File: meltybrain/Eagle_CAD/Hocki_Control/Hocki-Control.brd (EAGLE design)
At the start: 87 x 44 mm, 103 parts, among them J1 SM05B-SRSS-TB(LF)(SN), J2 SM05B-SRSS-TB(LF)(SN), U1 TEENSY_4.1, U10 TLV3502AIDCNR, U11 NL27WZ32USG, U12 NL27WZ32USG, U13 HMC1052L-TR, U14 LMV358, U15 IRF7509, U16 TMUX1219DCKR, U17 LMV358, U18 LMV358, U19 AP2210K-3.3TRG1, U2 ADXL375, U20 AP2210K-5.0TRG1, U3 ADXL375, U4 ADXL375, U5 ADXL375, U6 LMH6612MAX/NOPB, U7 LMH6612MAX/NOPB, U8 LMH6612MAX/NOPB, U9 LMH6612MAX/NOPB

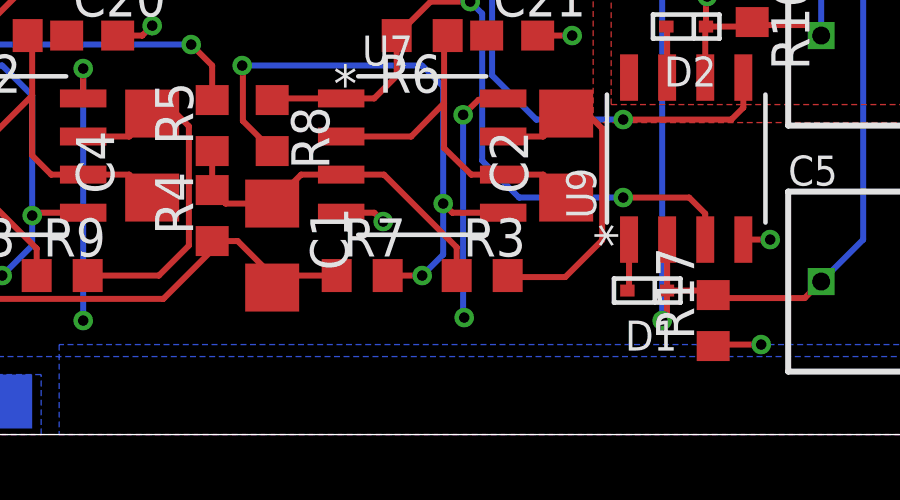
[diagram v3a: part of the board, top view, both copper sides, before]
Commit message: fixed 10k bandpass
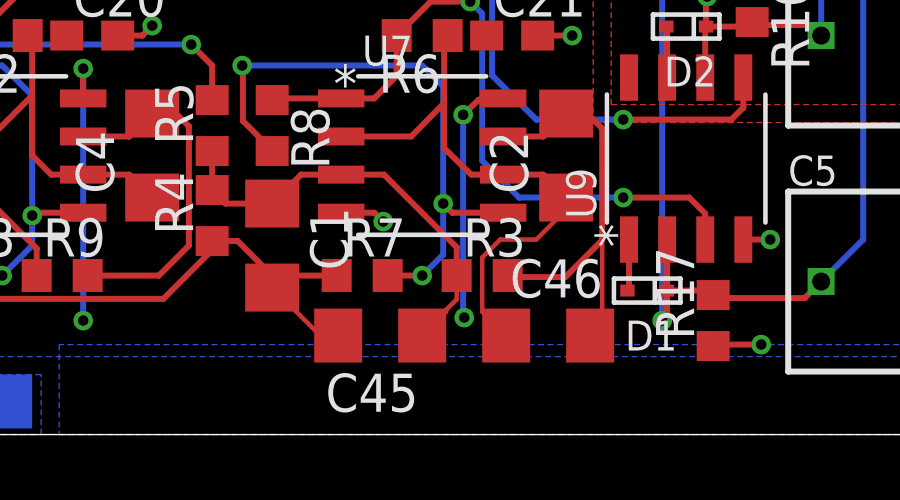
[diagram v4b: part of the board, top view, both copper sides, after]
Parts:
- added C45, C46: 47n, rcl:C1206
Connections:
- net 1.66V_REF_BUF: now also C45.2
- net 10K_FB: now also C46.2
- net 10K_IN: now also C45.1
- net N$4: now also C46.1
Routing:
- net N$4: track 12.5 -> 19.2 mm
- net 10K_FB: track 11.2 -> 14.6 mm
- net 1.66V_REF_BUF: track 29.0 -> 31.9 mm
- net 10K_IN: track 12.0 -> 14.5 mm
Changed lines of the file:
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@@
 <drawing>
 <settings>
-<setting alwaysvectorfont="yes"/>
+<setting alwaysvectorfont="no"/>
 <setting verticaltext="up"/>
 </settings>
@@
 <attribute name="VALUE" x="-26.205" y="-19.065" size="1.27" layer="27" rot="R270"/>
 </element>
+<element name="C45" library="rcl" library_urn="urn:adsk.eagle:library:334" package="C1206" package3d_urn="urn:adsk.eagle:package:23618/2" value="47n" x="6.3" y="-21.7" smashed="yes" rot="R180">
+<attribute name="NAME" x="7.57" y="-22.97" size="1.27" layer="25" rot="R180"/>
+<attribute name="POPULARITY" value="24" x="6.3" y="-21.7" size="1.778" layer="27" rot="R180" display="off"/>
+<attribute name="SPICEPREFIX" value="C" x="6.3" y="-21.7" size="1.778" layer="27" rot="R180" display="off"/>
+<attribute name="VALUE" x="7.57" y="-19.16" size="1.27" layer="27" rot="R180"/>
+</element>
+<element name="C46" library="rcl" library_urn="urn:adsk.eagle:library:334" package="C1206" package3d_urn="urn:adsk.eagle:package:23618/2" value="47n" x="11.9" y="-21.7" smashed="yes">
+<attribute name="NAME" x="10.63" y="-20.43" size="1.27" layer="25"/>
+<attribute name="POPULARITY" value="24" x="11.9" y="-21.7" size="1.778" layer="27" display="off"/>
+<attribute name="SPICEPREFIX" value="C" x="11.9" y="-21.7" size="1.778" layer="27" display="off"/>
+<attribute name="VALUE" x="10.63" y="-24.24" size="1.27" layer="27"/>
+</element>
 </elements>
 <signals>
@@
 <wire x1="12.471025" y1="-19.75" x2="13.7" y2="-18.521025" width="0.2" layer="1"/>
 <wire x1="13.7" y1="-18.521025" x2="13.7" y2="-14.8" width="0.2" layer="1"/>
+<contactref element="C46" pad="2"/>
+<wire x1="13.3" y1="-21.7" x2="13.7" y2="-21.3" width="0.1524" layer="1"/>
+<wire x1="13.7" y1="-21.3" x2="13.7" y2="-18.521025" width="0.1524" layer="1"/>
 </signal>
 <signal name="N$4">
@@
 <wire x1="10.4" y1="-16.335" x2="11.735" y2="-16.335" width="0.2" layer="1"/>
 <wire x1="11.735" y1="-16.335" x2="12.5" y2="-17.1" width="0.2" layer="1"/>
+<contactref element="C46" pad="1"/>
+<wire x1="10.5" y1="-21.7" x2="9.7068" y2="-20.9068" width="0.1524" layer="1"/>
+<wire x1="9.7068" y1="-20.9068" x2="9.7068" y2="-20.84865" width="0.1524" layer="1"/>
+<wire x1="9.7068" y1="-20.84865" x2="9.7" y2="-20.84185" width="0.1524" layer="1"/>
+<wire x1="9.7" y1="-19.1" x2="10.3" y2="-18.5" width="0.1524" layer="1"/>
+<wire x1="10.3" y1="-18.5" x2="11.5" y2="-18.5" width="0.1524" layer="1"/>
+<wire x1="11.5" y1="-18.5" x2="12.5" y2="-17.5" width="0.1524" layer="1"/>
+<wire x1="12.5" y1="-17.5" x2="12.5" y2="-17.1" width="0.1524" layer="1"/>
+<wire x1="9.7" y1="-20.84185" x2="9.7" y2="-19.1" width="0.1524" layer="1"/>
 </signal>
 <signal name="10K_IN">
@@
 <wire x1="1.15" y1="-17.3" x2="0.7" y2="-16.85" width="0.2" layer="1"/>
 <wire x1="0.7" y1="-16.85" x2="0.7" y2="-15.55" width="0.2" layer="1"/>
+<contactref element="C45" pad="1"/>
+<wire x1="7.7" y1="-21.7" x2="8.4932" y2="-20.9068" width="0.1524" layer="1"/>
+<wire x1="8.4932" y1="-20.9068" x2="8.4932" y2="-20.84865" width="0.1524" layer="1"/>
+<wire x1="8.85" y1="-20.49185" x2="8.85" y2="-19.7" width="0.1524" layer="1"/>
+<wire x1="8.4932" y1="-20.84865" x2="8.85" y2="-20.49185" width="0.1524" layer="1"/>
 </signal>
 <signal name="10K_OUT">
@@
 <wire x1="-10.523" y1="-20.477" x2="-11.1" y2="-19.9" width="0.2" layer="1"/>
 <wire x1="-0.927" y1="-20.477" x2="-10.523" y2="-20.477" width="0.2" layer="1"/>
+<contactref element="C45" pad="2"/>
+<wire x1="4.9" y1="-21.7" x2="4.3" y2="-21.7" width="0.1524" layer="1"/>
+<wire x1="4.3" y1="-21.7" x2="2.7" y2="-20.1" width="0.1524" layer="1"/>
 </signal>
 <signal name="N$2">

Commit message: forgot to save before pushing...
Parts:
- J1, J2: value SM05B-SRSS-TB(LF)(SN) -> SM03B-SRSS-TB(LF)(SN); device Hocki_Library:SM05B-SRSS-TB(LF)(SN) -> Hocki_Library:SM03B-SRSS-TB(LF)(SN)
- moved J1 9.45 mm to (-18.5, -22.2), flipped to the top
- moved J2 7.50 mm to (-24.5, -22.2), flipped to the top
- moved C42 6.04 mm to (-21.8, -19.8), turned to 0 degrees
- moved C44 5.10 mm to (-26.5, -15.1), turned to 180 degrees
- moved C18 3.58 mm to (-13.2, -23.4), turned to 0 degrees
- moved C41 2.21 mm to (-29.4, -17.6)
- moved U20 2.21 mm to (-26.5, -17.6)
- moved U16 1.41 mm to (-14.4, -20.8)
- moved R2 1.00 mm to (-17.4, -19.8)
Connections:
- removed net IR_BOTTOM_A0: J2.3, U1.35
- removed net IR_BOTTOM_A1: J2.4, U1.34
- removed net IR_TOP_A0: J1.3, U1.37
- removed net IR_TOP_A1: J1.4, U1.36
- net 5V: now also J1.S1, J1.S2, J2.S1, J2.S2
- net 9V: no longer J1.S1, J1.S2, J2.S1, J2.S2
- net GND: now also J1.3, J2.3; no longer J1.5, J2.5
- net IR_SEL: now also U1.37; no longer U1.33
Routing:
- net IR_TOP_A1: track 24.2 -> 0.00 mm
- net IR_BOTTOM_A0: track 24.1 -> 0.00 mm
- net IR_TOP_A0: track 23.6 -> 0.00 mm
- net IR_BOTTOM_A1: track 23.0 -> 0.00 mm
- net IR_BOTTOM: track 5.14 -> 10.8 mm, vias 1 -> 0
- net IR_SEL: track 31.0 -> 26.2 mm
- net 9V: track 8.87 -> 11.8 mm, vias 0 -> 2
- net GND: track 105.4 -> 103.1 mm, vias 70 -> 72
- net N$8: track 2.04 -> 3.07 mm
- net IR_TOP: track 7.36 -> 6.50 mm, vias 1 -> 0
- net VG_SIGNAL: track 12.1 -> 11.5 mm
- removed copper zone on layer 16, net 9V
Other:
- board size 87 x 44 mm -> 90 x 46 mm

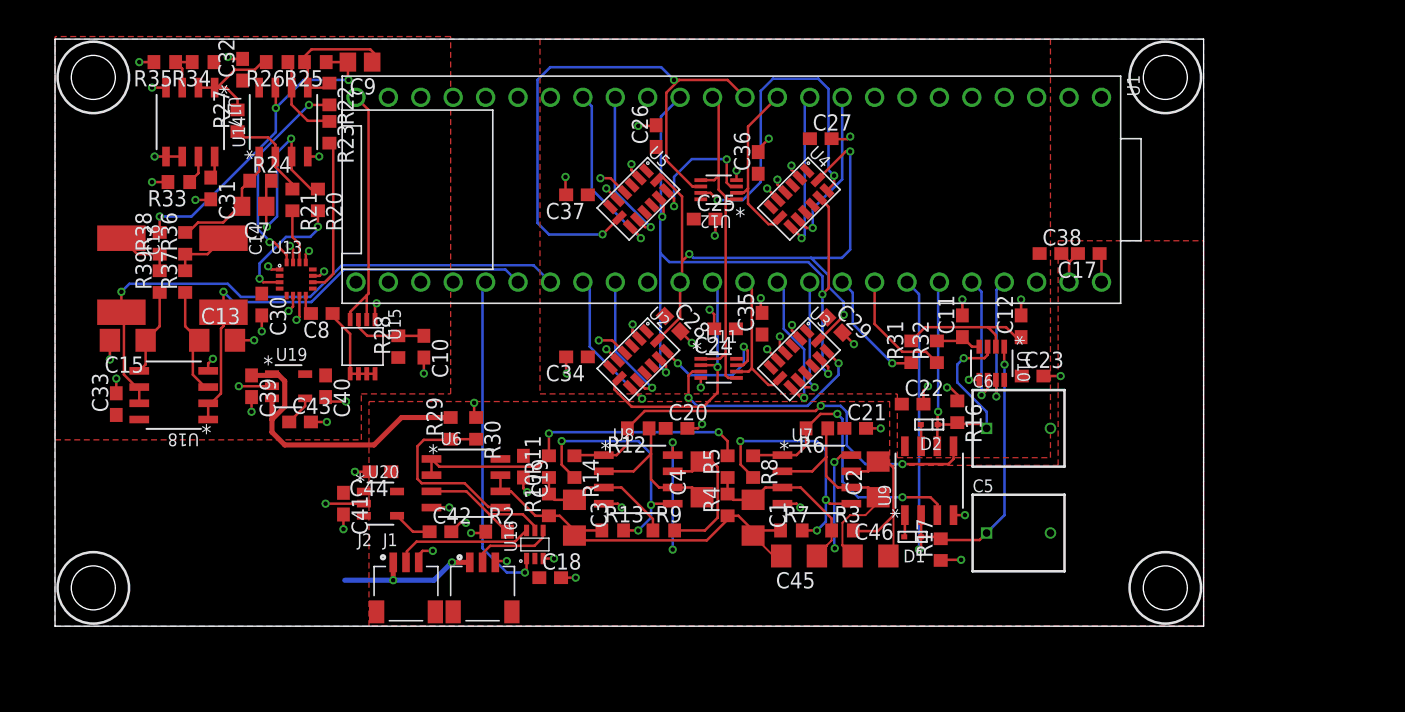
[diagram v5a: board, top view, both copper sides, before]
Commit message: power in
traces under capacitors be sketch...tried to avoid...
24-9 regulator is in
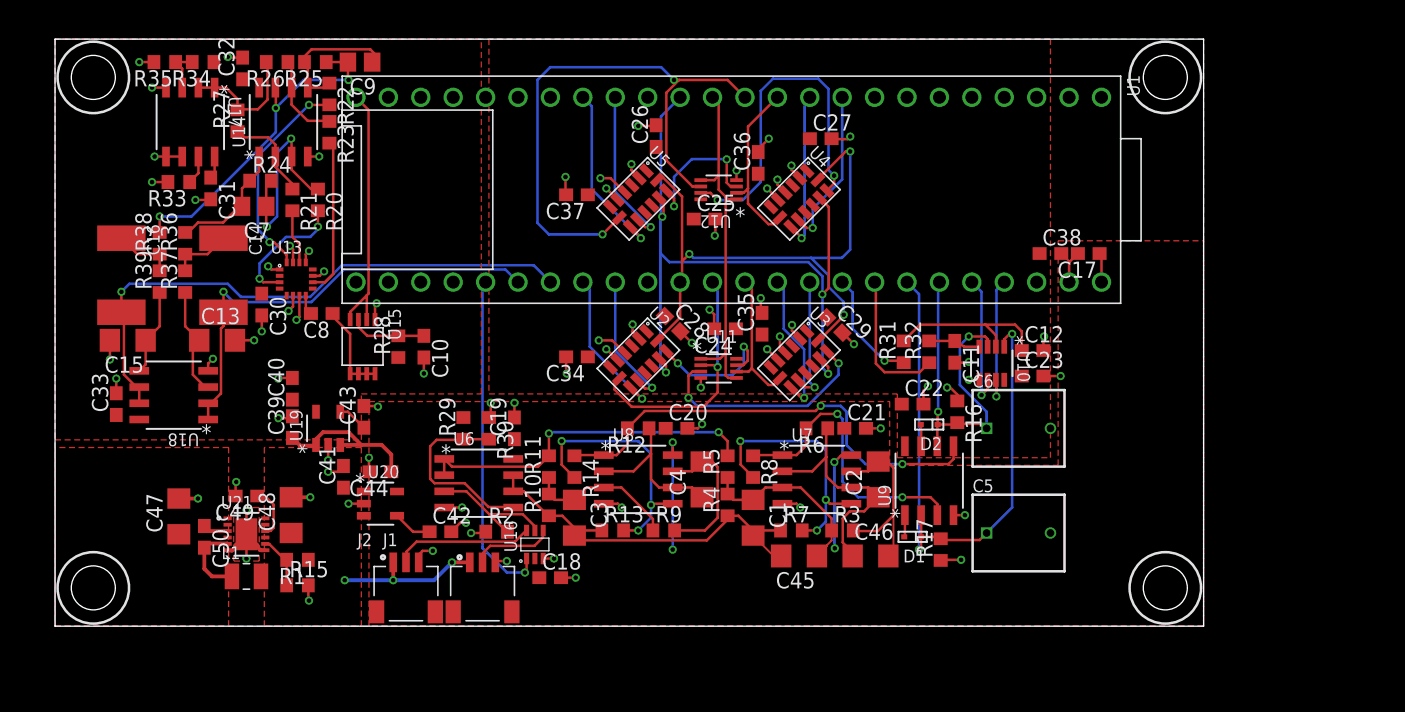
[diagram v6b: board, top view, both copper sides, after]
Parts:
- added C47: 4.7u, rcl:C1206
- added C48: 22u, rcl:C1206
- added C49: 1u, rcl:C0603
- added C50: 0.1u, rcl:C0603
- added L1: 4.7u, Hocki_Library:1007
- added R1: 324k, rcl:R0603
- added R15: 40.2k, rcl:R0603
- added U21: MAX20075ATCA/V+, Hocki_Library:12-TDFN
- moved C43 5.02 mm to (-27.8, -10.8), turned to 90 degrees
- moved U19 4.53 mm to (-30.6, -11.7), turned to 90 degrees
- moved C39 4.53 mm to (-33.4, -11.6), turned to 90 degrees
- moved C19 3.08 mm to (-16.0, -11.7), turned to 90 degrees
- moved C40 2.61 mm to (-33.4, -8.60), turned to 90 degrees
- moved C12 2.10 mm to (24.6, -5.60), turned to 0 degrees
- moved C41 2.10 mm to (-29.4, -15.5), turned to 90 degrees
- moved C11 2.09 mm to (18.5, -5.70), turned to 270 degrees
- moved R29 1.00 mm to (-20.0, -11.7)
- moved R30 1.00 mm to (-18.0, -11.7)
- moved U6 1.00 mm to (-18.8, -16.0)
- moved R32 0.60 mm to (16.5, -5.70)
- moved R31 0.60 mm to (14.5, -5.70)
- moved C32 0.10 mm to (-37.3, 16.5)
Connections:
- new net +24V: C47.1, U21.2, U21.4
- new net N$1: C50.1, U21.3
- new net N$12: R1.2, R15.1, U21.8
- new net N$3: C50.2, L1.1, U21.5
- new net N$6: C49.1, U21.10
- net 9V: now also C48.1, L1.2, R1.1, U21.9
- net GND: now also C47.2, C48.2, C49.2, R15.2, U21.13, U21.6, U21.7
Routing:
- net 5V: track 44.3 -> 32.5 mm
- net GND: track 103.1 -> 112.2 mm, vias 72 -> 78
- net N$3: track 0.00 -> 6.03 mm
- net N$12: track 0.00 -> 4.19 mm
- net N$6: track 0.00 -> 4.13 mm
- net 10K_PEAK: track 44.8 -> 47.4 mm
- net 10K_REF: track 11.2 -> 13.6 mm
- net N$1: track 0.00 -> 1.99 mm
- net N$22: track 9.42 -> 11.2 mm
- net 20K_PEAK: track 26.3 -> 27.5 mm
- net VG_SIGNAL_BUF: track 28.3 -> 27.3 mm
- net VG_SIGNAL: track 11.5 -> 10.5 mm
- net VREF/2: track 9.16 -> 9.96 mm
- net 1.66V_REF_BUF: track 31.9 -> 31.1 mm
- net 9V: vias 2 -> 3
- added copper zone on layer 1, net +24V
- added copper zone on layer 1, net 9V
- added copper zone on layer 1, net GND
